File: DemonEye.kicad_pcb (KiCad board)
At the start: 2 copper layers, 16.4 x 35.2 mm, 59 parts, among them CN1 PicoBlade 1x07 P1.25mm, Q1 CSD25501F3, Q2 CSD25501F3, Q3 CSD25501F3, Q4 CSD25501F3, Q5 CSD25501F3, U1 WS2814B

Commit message: Update .gitignore, DemonEye.kicad_pcb, DemonEye.kicad_prl, and 3 more files
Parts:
- removed D1, D2, D3, D4, D5: 13V, My Package_Leadless:DFN0603-2
- removed the R10 at (114.0, 65.9)
- removed the R11 at (111.4, 66.9)
- removed the R15 at (111.4, 67.9)
- removed the R18 at (114.0, 67.9)
- removed the R19 at (111.4, 68.9)
- removed the R23 at (111.4, 69.9)
- removed the R26 at (114.0, 69.9)
- removed R31, R34: 680R, My Resistors:R_0201_Dense
- removed the R7 at (111.4, 65.9)
- added C6: 22uF, My Capacitors:C_0603_Dense, F.Cu at (100.9, 71.1)
- added R28: 25k5, My Resistors:R_0201_Nominal, F.Cu at (103.1, 71.5)
- added R4: 1k0, My Resistors:R_0402_Nominal, F.Cu at (103.9, 65.1)
- added R5: 1k0, My Resistors:R_0402_Nominal, F.Cu at (103.9, 66.3)
- added R6: 1k0, My Resistors:R_0402_Nominal, F.Cu at (103.9, 67.5)
- added U2: LMZM23601, My Package_Leadless:Texas_SIL0010A_MicroSiP-10-1EP_3.8x3mm_P0.6mm_EP0.7x2.9mm, F.Cu at (106.3, 70.4)
- R1, R2: value 2k7 -> 1k0; footprint My Resistors:R_0201_Nominal -> My Resistors:R_0402_Nominal
- R10: renamed from R8; value 680R -> 100R
- R11: renamed from R9; value 680R -> 100R
- R12, R13, R14, R16: value 680R -> 100R
- R15: renamed from R17; value 680R -> 100R
- R17: renamed from R20; value 680R -> 100R
- R18: renamed from R21; value 680R -> 100R
- R19: renamed from R22; value 680R -> 100R
- R20: renamed from R24; value 680R -> 100R
- R21: renamed from R25; value 680R -> 100R
- R22: renamed from R28; value 680R -> 100R
- R23: renamed from R29; value 680R -> 100R
- R24: renamed from R30; value 680R -> 100R
- R25: renamed from R32; value 680R -> 100R
- R26: renamed from R33; value 680R -> 100R
- R27: value 680R -> 249k; footprint My Resistors:R_0201_Dense -> My Resistors:R_0201_Nominal
- R3: value 680R -> 1k0; footprint My Resistors:R_0201_Dense -> My Resistors:R_0402_Nominal
- R7: renamed from R4; value 680R -> 100R
- R8: renamed from R5; value 680R -> 100R
- R9: renamed from R6; value 680R -> 100R
- U1: value WS2814B -> WS2814F; footprint Package_SO:SSOP-10_3.9x4.9mm_P1.00mm -> My Package_SO:FSOP-8_3.25x1.65mm_P0.8mm
- moved R27 9.30 mm to (102.1, 71.5), turned to -90 degrees
- moved R3 7.59 mm to (103.9, 63.9), turned to 180 degrees
- moved C3 6.20 mm to (109.2, 68.6)
- moved C1 5.08 mm to (110.3, 65.5)
- moved C5 4.53 mm to (103.6, 69.4), turned to -90 degrees
- moved C4 4.46 mm to (102.2, 69.4), turned to -90 degrees
- moved C2 4.25 mm to (109.2, 71.2), turned to -90 degrees
- moved R1 3.89 mm to (102.3, 73.6), turned to 90 degrees
- moved D10 3.54 mm to (110.3, 64.0), turned to 180 degrees
- moved R2 2.84 mm to (107.4, 67.8)
- moved R14 2.81 mm to (111.3, 67.9), turned to -90 degrees
- moved R19 2.81 mm to (111.3, 69.9), turned to -90 degrees
- moved R24 2.81 mm to (111.3, 71.9), turned to -90 degrees
- moved R9 2.81 mm to (111.3, 65.9), turned to -90 degrees
- moved D7 2.53 mm to (111.8, 73.1)
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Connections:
- net /+12V_{SW} renamed /+V_{OUT_{SW}}
- C4 pad 1: +12V -> V_{OUT}
- C5 pad 1: +12V -> V_{OUT}
- CN1 pad 5: /D_{IN} -> /D_{OUT}
- CN1 pad 7: /D_{OUT} -> /D_{IN}
- Q1 pad 2: +12V -> V_{OUT}
- Q2 pad 1: /OUTR -> /RedG
- Q3 pad 1: /OUTG -> /GreenG
- Q4 pad 1: /OUTB -> /BlueG
- Q5 pad 1: /OUTW -> /WhiteG
- R27 pad 1: /White3 -> /FB
- R27 pad 2: GND -> V_{OUT}
- R3 pad 1: /Red4 -> /OUTR
- R3 pad 2: GND -> /RedG
- U1 pad 4: /OUTW -> GND
- U1 pad 5: GND -> /D_{OUT}
- U1 pad 6: /D_{OUT} -> /D_{IN}
- U1 pad 7: GND -> /V_{DD}
- U1 pad 8: /D_{IN} -> /OUTW
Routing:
- net /+V_{OUT_{SW}}: track 28.9 -> 15.8 mm
- net /FB: track 0.00 -> 6.31 mm
- net /V_{DD}: track 9.55 -> 4.04 mm
- net /OUTB: track 3.78 -> 0.00 mm
- net /OUTR: track 3.70 -> 0.00 mm
- net /OUTG: track 3.69 -> 0.00 mm
- net /D_{OUT}: track 7.30 -> 10.2 mm
- net /OUTW: track 3.86 -> 6.60 mm
- net V_{OUT}: track 0.00 -> 2.18 mm
- net +12V: track 10.4 -> 8.34 mm
- net /Red3: track 1.35 -> 2.61 mm
- net /D_{IN}: track 9.84 -> 11.0 mm
- net /Blue3: track 10.7 -> 9.60 mm
- net /Green3: track 7.62 -> 6.55 mm
- net /SRH: track 8.60 -> 9.65 mm
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- added copper zone on F.Cu, net /BlueG
- added copper zone on F.Cu, net /D_{IN}
- added copper zone on F.Cu, net /D_{OUT}
- added copper zone on F.Cu, net /GreenG
- added copper zone on F.Cu, net /OUTB
- added copper zone on F.Cu, net /OUTG
- added copper zone on F.Cu, net /OUTR
- added copper zone on F.Cu, net /OUTW
- added copper zone on F.Cu, net /RedG
- added copper zone on F.Cu, net /V_{DD}
- added copper zone on F.Cu, net /WhiteG
- added copper zone on F.Cu, net V_{OUT}
- removed copper zone on F.Cu, net /Blue3
- removed copper zone on F.Cu, net /Green3
- removed copper zone on F.Cu, net /White3
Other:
- board size 16.4 x 35.2 mm -> 16 x 35.2 mm

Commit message: v0.4.0.0
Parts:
- removed C4, C5, C6: 22uF, My Capacitors:C_0603_Dense
- removed D10: 3V, My Package_Leadless:DFN1006-2
- removed the R11 at (113.5, 65.9)
- removed the R12 at (111.9, 66.9)
- removed R14, R15, R16, R17, R18, R19, R20, R21, R22, R23, R24, R25, R26: 100R, My Resistors:R_0201_Dense
- added Q10: BC807-25QAZ, My Package_Leadless:DFN1010D-3, F.Cu at (103.9, 70.7)
- added Q6: BC807-25QAZ, My Package_Leadless:DFN1010D-3, F.Cu at (105.5, 64.3)
- added Q8: BC807-25QAZ, My Package_Leadless:DFN1010D-3, F.Cu at (105.5, 66.5)
- added Q9: BC807-25QAZ, My Package_Leadless:DFN1010D-3, F.Cu at (104.7, 68.6)
- C2, C3: value 22uF -> 10uF
- CN1: footprint My Connectors:Molex_PicoBlade_53261-0771_1x07_P1.25mm_Horizontal_SMD -> My Connectors:Molex_PicoBlade_53261-0671_1x06_P1.25mm_Horizontal_SMD
- R10, R7, R8, R9: value 100R -> 3R48; footprint My Resistors:R_0201_Dense -> My Resistors:R_0402_Nominal
- R11: renamed from R27; value 249k -> 162k
- R12: renamed from R28; value 25k5 -> 12k7
- R13: value 100R -> 33R; footprint My Resistors:R_0201_Dense -> My Resistors:R_0201_Nominal
- U2: value LMZM23601 -> TLV76701DRVx; footprint My Package_Leadless:Texas_SIL0010A_MicroSiP-10-1EP_3.8x3mm_P0.6mm_EP0.7x2.9mm -> My Package_Leadless:WSON-6-1EP_2x2mm_P0.65mm_EP1x1.6mm
- moved R10 11.0 mm to (102.5, 70.7), turned to 90 degrees
- moved R8 8.96 mm to (104.1, 66.5)
- moved R9 8.48 mm to (103.3, 68.6), turned to 90 degrees
- moved R7 7.80 mm to (104.1, 64.3)
- moved R11 6.84 mm to (108.8, 69.9), turned to 180 degrees
- moved R12 5.73 mm to (108.8, 70.8), turned to 0 degrees
- moved U2 4.66 mm to (111.0, 70.1), turned to 0 degrees
- moved C2 3.96 mm to (113.0, 70.0)
- moved U1 3.81 mm to (110.8, 65.5)
- moved R4 3.80 mm to (107.5, 66.5)
- moved R6 3.75 mm to (105.8, 70.7)
- moved R3 3.58 mm to (107.5, 64.3)
- moved Q5 3.30 mm to (101.4, 70.7)
- moved R5 3.29 mm to (106.7, 68.1)
- moved Q1 3.26 mm to (101.4, 71.9), turned to 90 degrees
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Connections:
- C3 pad 1: +12V -> V_{OUT}
- CN1 pad 4: GND -> /D_{OUT}
- CN1 pad 5: /D_{OUT} -> GND
- CN1 pad 6: GND -> /D_{IN}
- LED3 pad 5: /White3 -> GND
- LED3 pad 6: /Blue3 -> GND
- LED3 pad 7: /Green3 -> GND
- LED3 pad 8: /Red3 -> GND
- Q2 pad 2: /+V_{OUT_{SW}} -> /RedS
- Q3 pad 2: /+V_{OUT_{SW}} -> /GreenS
- Q4 pad 2: /+V_{OUT_{SW}} -> /BlueS
- Q5 pad 2: /+V_{OUT_{SW}} -> /WhiteS
- R10 pad 1: /Red4 -> /+V_{OUT_{SW}}
- R10 pad 2: GND -> /WhiteS
- R13 pad 1: /Green3 -> /D_{OUT}
- R13 pad 2: GND -> /DOUT
- R2 pad 2: +12V -> V_{OUT}
- R7 pad 1: /Red4 -> /+V_{OUT_{SW}}
- R7 pad 2: GND -> /RedS
- R8 pad 1: /Red4 -> /+V_{OUT_{SW}}
- R8 pad 2: GND -> /GreenS
- R9 pad 1: /Red4 -> /+V_{OUT_{SW}}
- R9 pad 2: GND -> /BlueS
- U1 pad 5: /D_{OUT} -> /DOUT
- U2 pad 1: GND -> V_{OUT}
- U2 pad 2: unconnected-(U2-MODE/SYNC-Pad2) -> /FB
- U2 pad 3: +12V -> GND
- U2 pad 5: unconnected-(U2-PG-Pad5) -> GND
- U2 pad 6: V_{OUT} -> +12V
- U2 pad 7: /FB -> GND
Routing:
- net /White3: track 12.7 -> 0.00 mm
- net /Blue3: track 9.60 -> 0.00 mm
- net /Green3: track 6.55 -> 0.00 mm
- net V_{OUT}: track 2.18 -> 7.78 mm
- net /FB: track 6.31 -> 1.96 mm
- net /D_{IN}: track 11.0 -> 15.0 mm
- net /GreenG: track 0.25 -> 4.21 mm
- net /D_{OUT}: track 10.2 -> 14.0 mm
- net /BlueG: track 0.25 -> 3.99 mm
- net /OUTW: track 6.60 -> 10.3 mm
- net /WhiteG: track 0.25 -> 3.80 mm
- net /RedG: track 0.25 -> 3.80 mm
- net +12V: track 8.34 -> 11.8 mm
- net /OUTB: track 0.00 -> 3.43 mm
- net /Red4: track 2.65 -> 0.00 mm
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- added copper zone on F.Cu, net /+V_{OUT_{SW}}
- added copper zone on F.Cu, net /Blue0
- added copper zone on F.Cu, net /BlueS
- added copper zone on F.Cu, net /Green0
- added copper zone on F.Cu, net /GreenS
- added copper zone on F.Cu, net /Red0
- added copper zone on F.Cu, net /RedS
- added copper zone on F.Cu, net /White0
- added copper zone on F.Cu, net /WhiteS
- removed copper zone on F.Cu, net /D_{IN}
- removed copper zone on F.Cu, net /D_{OUT}
- removed copper zone on F.Cu, net /OUTB
- removed copper zone on F.Cu, net /OUTG
- removed copper zone on F.Cu, net /OUTR
- removed copper zone on F.Cu, net /OUTW
- removed copper zone on F.Cu, net /Red4
- removed copper zone on F.Cu, net /V_{DD}
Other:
- board text added: "v0.4.0.0"
- board text removed: "v0.3.0.0"

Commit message: Update ConstantCurrentWithThermalFoldbackDesign.txt, DemonEye.kicad_pcb, DemonEye.kicad_prl, and 3 more files
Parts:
- removed Q10: BC807-25QAZ, My Package_Leadless:DFN1010D-3
- added Q7: BC807-25QAZ, My Package_Leadless:DFN1010D-3, F.Cu at (105.3, 69.2)
- added R14: 1k0, My Resistors:R_0402_Nominal, F.Cu at (106.7, 68.9)
- added R15: 5R6, My Resistors:R_0402_Nominal, F.Cu at (102.5, 71.1)
- added R16: 511, My Resistors:R_0201_Dense, F.Cu at (101.6, 70.5)
- added R17: 1k0, My Resistors:R_0402_Nominal, F.Cu at (106.3, 71.1)
- added R18: 160, My Resistors:R_0201_Dense, F.Cu at (114.1, 60.2)
- added R19: 160, My Resistors:R_0201_Dense, F.Cu at (114.1, 60.8)
- added R20: 160, My Resistors:R_0201_Dense, F.Cu at (114.1, 61.4)
- added R21: 160, My Resistors:R_0201_Dense, F.Cu at (114.1, 62.0)
- added R22: 160, My Resistors:R_0201_Dense, F.Cu at (114.1, 62.6)
- added R23: 160, My Resistors:R_0201_Dense, F.Cu at (114.1, 63.2)
- added R24: 160, My Resistors:R_0201_Dense, F.Cu at (114.1, 63.8)
- added R25: 160, My Resistors:R_0201_Dense, F.Cu at (114.1, 64.4)
- added TH1: 4k7, My Resistors:TH_0402_Nominal, F.Cu at (105.2, 64.6)
- added TH2: 4k7, My Resistors:TH_0402_Nominal, F.Cu at (104.3, 66.8)
- added TH3: 4k7, My Resistors:TH_0402_Nominal, F.Cu at (104.0, 69.0)
- added TH4: 4k7, My Resistors:TH_0402_Nominal, F.Cu at (103.5, 71.2)
- CN1: value PicoBlade 1x07 P1.25mm -> PicoBlade 1x06 P1.25mm
- Q3, Q5: value CSD25501F3 -> BC807-25QAZ; footprint My Package_Leadless:Texas_-YJN_0.7x0.6mm_PicoStar -> My Package_Leadless:DFN1010D-3
- Q6, Q8: value BC807-25QAZ -> CSD25501F3; footprint My Package_Leadless:DFN1010D-3 -> My Package_Leadless:Texas_-YJN_0.7x0.6mm_PicoStar
- R10, R7: value 3R48 -> 511; footprint My Resistors:R_0402_Nominal -> My Resistors:R_0201_Dense
- R11: value 162k -> 1k0; footprint My Resistors:R_0201_Nominal -> My Resistors:R_0402_Nominal
- R12: value 12k7 -> 5R6; footprint My Resistors:R_0201_Nominal -> My Resistors:R_0402_Nominal
- R13: value 33R -> 511; footprint My Resistors:R_0201_Nominal -> My Resistors:R_0201_Dense
- R3: value 1k0 -> 33R; footprint My Resistors:R_0402_Nominal -> My Resistors:R_0201_Nominal
- R4: value 1k0 -> 1M43; footprint My Resistors:R_0402_Nominal -> My Resistors:R_0201_Dense
- R5: value 1k0 -> 105k; footprint My Resistors:R_0402_Nominal -> My Resistors:R_0201_Dense
- R6: value 1k0 -> 5R6
- R8: value 3R48 -> 1k0
- R9: value 3R48 -> 5R6
- moved R13 11.7 mm to (102.0, 68.3), turned to -90 degrees
- moved Q8 6.60 mm to (101.4, 71.6), turned to 180 degrees
- moved R3 6.60 mm to (113.6, 66.7)
- moved R6 6.47 mm to (104.1, 64.5), turned to 90 degrees
- moved Q6 6.30 mm to (101.8, 69.4), turned to 180 degrees
- moved R12 6.22 mm to (102.9, 68.9), turned to 90 degrees
- moved Q1 6.06 mm to (107.4, 71.1), turned to 180 degrees
- moved Q5 5.69 mm to (105.7, 67.0), turned to 0 degrees
- moved R10 4.60 mm to (102.4, 66.1), turned to -90 degrees
- moved R8 4.28 mm to (107.9, 64.5), turned to -90 degrees
- moved Q3 4.15 mm to (106.5, 64.8), turned to 0 degrees
- moved R11 3.67 mm to (107.1, 66.7), turned to -90 degrees
- moved R4 3.29 mm to (108.4, 69.6), turned to 90 degrees
- moved R5 3.05 mm to (108.4, 70.6), turned to 90 degrees
- moved Q9 2.81 mm to (104.9, 71.4)
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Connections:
- LED3 pad 8: GND -> /Red3
- Q2 pad 1: /RedG -> /Gate_{R}
- Q2 pad 2: /RedS -> /Source_{R}
- Q3 pad 1: /GreenG -> /Base_{R}
- Q3 pad 2: /GreenS -> /+V_{OUT_{SW}}
- Q3 pad 3: /Green0 -> /Gate_{R}
- Q4 pad 1: /BlueG -> /Gate_{G}
- Q4 pad 2: /BlueS -> /Source_{G}
- Q4 pad 3: /Blue0 -> /Green0
- Q5 pad 1: /WhiteG -> /Base_{G}
- Q5 pad 2: /WhiteS -> /+V_{OUT_{SW}}
- Q5 pad 3: /White0 -> /Gate_{G}
- Q6 pad 1: /RedS -> /Gate_{B}
- Q6 pad 2: /+V_{OUT_{SW}} -> /Source_{B}
- Q6 pad 3: /RedG -> /Blue0
- Q8 pad 1: /GreenS -> /Gate_{W}
- Q8 pad 2: /+V_{OUT_{SW}} -> /Source_{W}
- Q8 pad 3: /GreenG -> /White0
- Q9 pad 1: /BlueS -> /Base_{W}
- Q9 pad 3: /BlueG -> /Gate_{W}
- R10 pad 1: /+V_{OUT_{SW}} -> /Base_{G}
- R10 pad 2: /WhiteS -> /Source_{G}
- R11 pad 1: /FB -> /OUTG
- R11 pad 2: V_{OUT} -> /Gate_{G}
- R12 pad 1: GND -> /+V_{OUT_{SW}}
- R12 pad 2: /FB -> /Source_{B}
- R13 pad 1: /D_{OUT} -> /Base_{B}
- R13 pad 2: /DOUT -> /Source_{B}
- R3 pad 1: /OUTR -> /D_{OUT}
- R3 pad 2: /RedG -> /DOUT
- R4 pad 1: /OUTG -> /FB
- R4 pad 2: /GreenG -> V_{OUT}
- R5 pad 1: /OUTB -> GND
- R5 pad 2: /BlueG -> /FB
- R6 pad 1: /OUTW -> /+V_{OUT_{SW}}
- R6 pad 2: /WhiteG -> /Source_{R}
- R7 pad 1: /+V_{OUT_{SW}} -> /Base_{R}
- R7 pad 2: /RedS -> /Source_{R}
- R8 pad 1: /+V_{OUT_{SW}} -> /OUTR
- R8 pad 2: /GreenS -> /Gate_{R}
- R9 pad 2: /BlueS -> /Source_{G}
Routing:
- net /+V_{OUT_{SW}}: track 17.9 -> 6.04 mm
- net V_{OUT}: track 7.78 -> 0.00 mm
- net /Gate_{R}: track 0.00 -> 5.43 mm
- net /Gate_{B}: track 0.00 -> 5.43 mm
- net /Gate_{G}: track 0.00 -> 5.43 mm
- net /Gate_{W}: track 0.00 -> 5.43 mm
- net /GreenG: track 4.21 -> 0.00 mm
- net /BlueG: track 3.99 -> 0.00 mm
- net /WhiteG: track 3.80 -> 0.00 mm
- net /RedG: track 3.80 -> 0.00 mm
- net /Base_{R}: track 0.00 -> 3.62 mm
- net /Base_{W}: track 0.00 -> 3.62 mm
- net /Base_{G}: track 0.00 -> 3.62 mm
- net /Base_{B}: track 0.00 -> 3.62 mm
- net /Source_{W}: track 0.00 -> 1.67 mm
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- added copper zone on F.Cu, net /FB
- added copper zone on F.Cu, net /Red3
- removed copper zone on F.Cu, net /Blue0
- removed copper zone on F.Cu, net /BlueG
- removed copper zone on F.Cu, net /BlueS
- removed copper zone on F.Cu, net /Green0
- removed copper zone on F.Cu, net /GreenG
- removed copper zone on F.Cu, net /GreenS
- removed copper zone on F.Cu, net /RedG
- removed copper zone on F.Cu, net /RedS
- removed copper zone on F.Cu, net /White0
- removed copper zone on F.Cu, net /WhiteG
- removed copper zone on F.Cu, net /WhiteS
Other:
- outline, holes or cut-outs redrawn
- board text added: "v0.4.1.0"
- board text removed: "v0.4.0.0"

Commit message: Update DemonEye.kicad_pcb, corrected FemtoFET footprint
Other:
- board text added: "v0.4.1.1"
- board text removed: "v0.4.1.0"

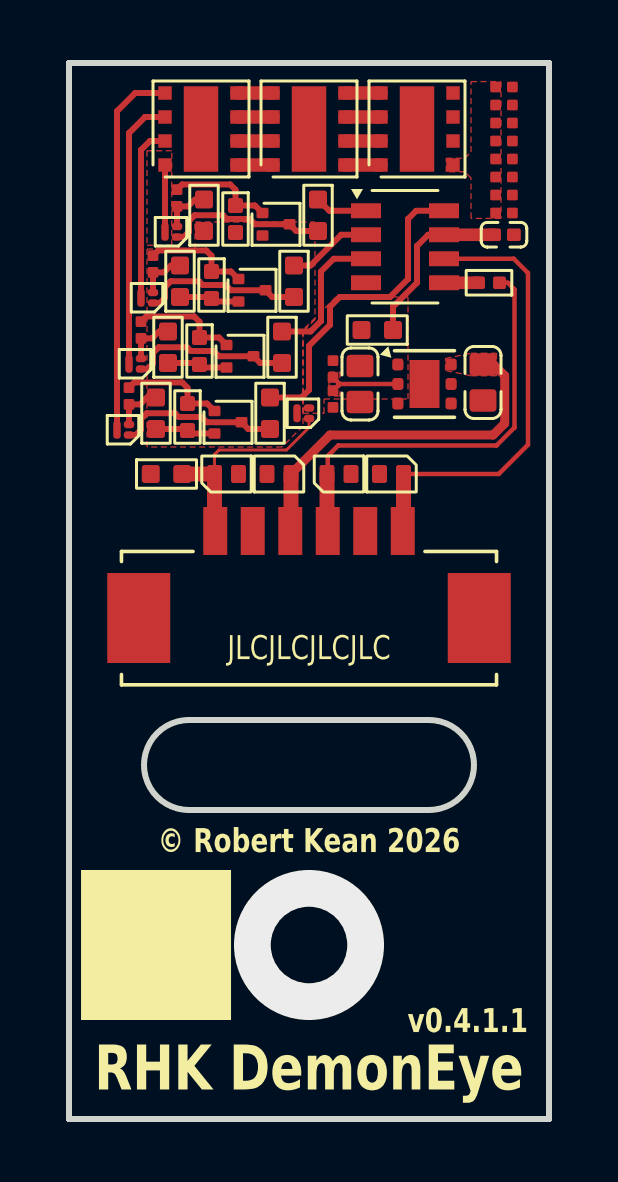
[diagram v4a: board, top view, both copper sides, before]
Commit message: improved spacing on components between pad and silkscreen.  required some shifting of components on board
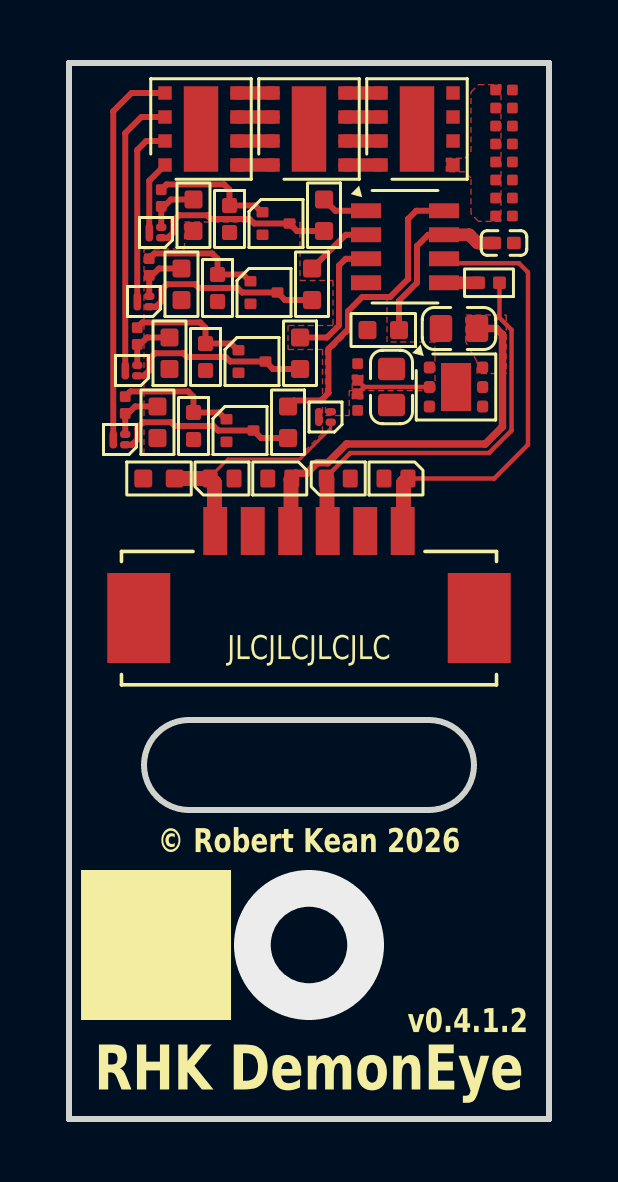
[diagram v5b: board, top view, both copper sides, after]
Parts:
- moved C2 1.97 mm to (112.6, 68.2), turned to 180 degrees
- moved C3 1.05 mm to (110.3, 70.2)
- moved U2 1.05 mm to (112.5, 70.2)
- moved R4 0.83 mm to (109.2, 69.7)
- moved R5 0.83 mm to (109.2, 70.7)
- moved Q1 0.76 mm to (108.2, 71.2)
- moved R17 0.67 mm to (106.9, 71.4)
- moved R14 0.63 mm to (107.3, 69.1)
- moved R11 0.61 mm to (107.7, 66.8)
- moved R7 0.53 mm to (102.7, 63.9)
- moved Q2 0.50 mm to (102.5, 65.0)
- moved Q9 0.49 mm to (105.3, 71.7)
- moved Q7 0.44 mm to (105.7, 69.3)
- moved Q5 0.41 mm to (106.1, 67.0)
- moved TH4 0.36 mm to (103.8, 71.5)
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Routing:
- net /+V_{OUT_{SW}}: track 6.04 -> 0.00 mm
- net +12V: track 12.2 -> 13.5 mm
- net /Gate_{W}: track 5.43 -> 6.18 mm
- net /Gate_{G}: track 5.43 -> 6.18 mm
- net /Gate_{R}: track 5.43 -> 6.18 mm
- net /Gate_{B}: track 5.43 -> 6.18 mm
- net /D_{OUT}: track 14.4 -> 13.7 mm
- net /OUTG: track 2.82 -> 2.27 mm
- net /Base_{G}: track 3.62 -> 4.15 mm
- net /Base_{B}: track 3.62 -> 4.15 mm
- net /Base_{R}: track 3.62 -> 4.15 mm
- net /Base_{W}: track 3.62 -> 4.15 mm
- removed copper zone on F.Cu, net /Red0
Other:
- board text added: "v0.4.1.2"
- board text removed: "v0.4.1.1"
